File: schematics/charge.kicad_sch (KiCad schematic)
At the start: 59 parts, among them K1 AZ9861-1C-24DC2R1, Q2 NPN, Q3 NPN, T1 Transformer_1P_1S, U12 UA741, U3 VO2611, U4 VO2611, U5 UA741, U6 IL300, U7 UA741, U8 LM393, U9 VO2611

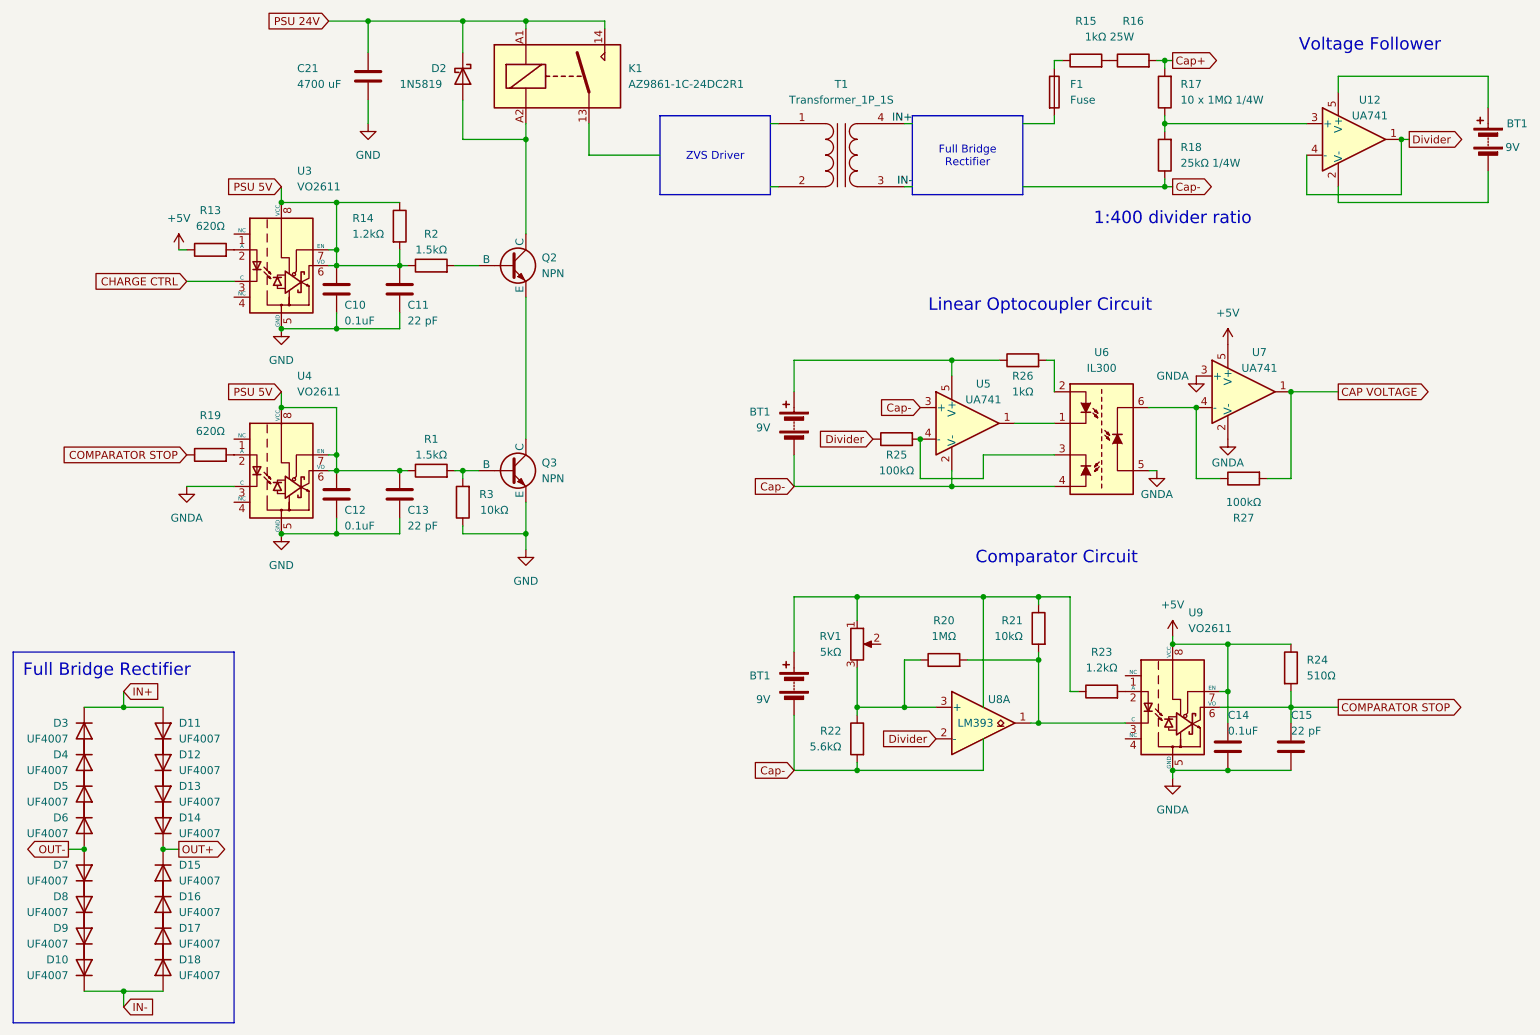
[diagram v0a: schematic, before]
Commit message: Fixed optocoupler wiring bug
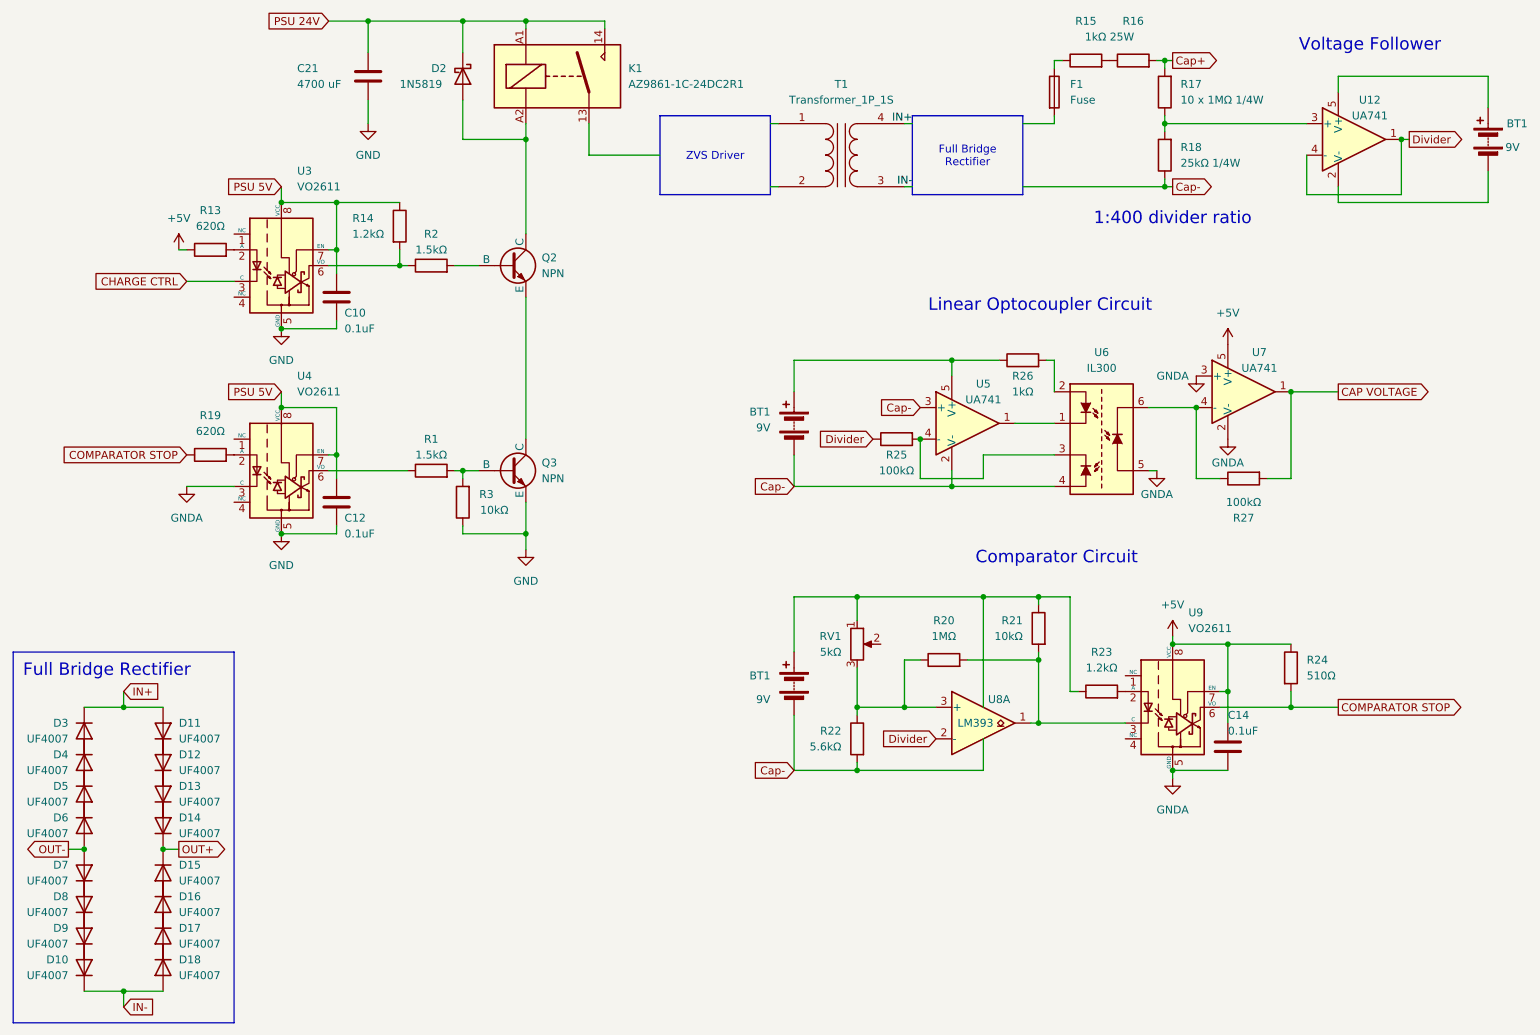
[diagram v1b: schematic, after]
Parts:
- removed C11, C13, C15: 22 pF, symbol Device:C
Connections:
- net PSU 5V: no longer R1.1, R14.2, R2.1, U3.6 (VO), U4.6 (VO)
- new net: R1.1, U4.6 (VO)
- new net: R14.2, R2.1, U3.6 (VO)
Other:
- moved on the sheet: C10, C12
